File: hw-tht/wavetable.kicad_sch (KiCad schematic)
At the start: 33 parts, among them J8 SJ1-3535NG-GR, J9 Waveblaster, U10 74AHCT126, U11 NE5532, U7 74AHC00

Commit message: Mixer: +6 dB Waveblaster gain (R10/R11/R19/R20 20k, C30/C31 47p)
Waveblaster daughterboards put out about 1-1.2 Vrms full scale (DreamBlaster X2:
AK4388, 1.13 Vrms) against the PCM5100A's 2.1 Vrms, so with unity WT gain MIDI
was 5-6 dB quieter than PCM at RV1 max.

Raise the summer's feedback and PCM input resistors from 10k to 20k on both
boards: WT gain at RV1 max = 20k/10k = 2 (+6 dB), PCM 20k/20.47k (-0.2 dB, as
before). The daughterboard load (about 4.8k at RV1 max) and the pot taper stay
unchanged. C30/C31 100p -> 47p keeps the feedback pole at ~170 kHz.

BOM-only change (no copper change): schematic values/fields, PCB values,
BOM-THT/BOM-SMD lines with the previous values in the notes, DigiKey upload
files (1x/10x), schematic PDFs. SMD C30/C31 get an LCSC field (C14857,
CL21C470JBANNNC) because DigiKey only stocks the 100 V CL21C470JC61PNC.
README mixer text updated; the THT diagram now shows R14 on the J9 side of C22
and R12 joined to the summing node. ERC 0, DRC 0 with schematic parity.

Co-Authored-By: Claude Opus 5.5 <noreply@anthropic.com>
Claude-Session: https://claude.ai/code/session_011utN3x8yYUNDvkpGCEq5yD
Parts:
- C30, C31: value 100pF C0G -> 47pF C0G; Alternatives TDK FG28C0G1H101JNT06 (DK 445-173472-1-ND). -> TDK FG28C0G1H470JNT06 (DK 445-173499-1-ND); LCSC C123159 (T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; DigiKey BC1042CT-ND -> BC1038CT-ND; LCSC C400081 (TORCH CC4-0805-CG-100V-100PF-J (5.08 mm pitch)) -> C3690607; MPN K101J15C0GF5TH5 -> K470J15C0GF5TH5
- R10, R11, R19, R20: value 10K -> 20K; DigiKey 10.0KXBK-ND -> 20.0KXBK-ND; LCSC C1519255 -> C1364283; MPN MFR-25FBF52-10K -> MFR-25FBF52-20K
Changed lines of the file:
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@@
 			)
 		)
-		(property "Value" "10K"
+		(property "Value" "20K"
 			(at 167.64 93.98 90)
 			(show_name no)
@@
 			)
 		)
-		(property "Description" "10k 1/4W 1% metal film"
+		(property "Description" "20k 1/4W 1% metal film"
 			(at 167.64 91.44 0)
 			(hide yes)
@@
 			)
 		)
-		(property "MPN" "MFR-25FBF52-10K"
+		(property "MPN" "MFR-25FBF52-20K"
 			(at 167.64 91.44 0)
 			(hide yes)
@@
 			)
 		)
-		(property "DigiKey" "10.0KXBK-ND"
+		(property "DigiKey" "20.0KXBK-ND"
 			(at 167.64 91.44 0)
 			(hide yes)
@@
 			)
 		)
-		(property "LCSC" "C1519255"
+		(property "LCSC" "C1364283"
 			(at 167.64 91.44 0)
 			(hide yes)
@@
 			)
 		)
-		(property "Value" "10K"
+		(property "Value" "20K"
 			(at 193.04 88.04 90)
 			(show_name no)
@@
 			)
 		)
-		(property "Description" "10k 1/4W 1% metal film"
+		(property "Description" "20k 1/4W 1% metal film"
 			(at 187.96 86.36 0)
 			(hide yes)
@@
 			)
 		)
-		(property "MPN" "MFR-25FBF52-10K"
+		(property "MPN" "MFR-25FBF52-20K"
 			(at 187.96 86.36 0)
 			(hide yes)
@@
 			)
 		)
-		(property "DigiKey" "10.0KXBK-ND"
+		(property "DigiKey" "20.0KXBK-ND"
 			(at 187.96 86.36 0)
 			(hide yes)
@@
 			)
 		)
-		(property "LCSC" "C1519255"
+		(property "LCSC" "C1364283"
 			(at 187.96 86.36 0)
 			(hide yes)
@@
 			)
 		)
-		(property "Value" "100pF C0G"
+		(property "Value" "47pF C0G"
 			(at 186.69 77.47 90)
 			(show_name no)
@@
 			)
 		)
-		(property "Description" "100pF 50V C0G radial MLCC"
+		(property "Description" "47pF 50V C0G radial MLCC"
 			(at 187.96 81.28 0)
 			(hide yes)
@@
 			)
 		)
-		(property "MPN" "K101J15C0GF5TH5"
+		(property "MPN" "K470J15C0GF5TH5"
 			(at 187.96 81.28 0)
 			(hide yes)
@@
 			)
 		)
-		(property "DigiKey" "BC1042CT-ND"
+		(property "DigiKey" "BC1038CT-ND"
 			(at 187.96 81.28 0)
 			(hide yes)
@@
 			)
 		)
-		(property "LCSC" "C400081 (TORCH CC4-0805-CG-100V-100PF-J (5.08 mm pitch))"
+		(property "LCSC" "C3690607"
 			(at 187.96 81.28 0)
 			(hide yes)
@@
 			)
 		)
-		(property "Alternatives" "TDK FG28C0G1H101JNT06 (DK 445-173472-1-ND)."
+		(property "Alternatives" "TDK FG28C0G1H470JNT06 (DK 445-173499-1-ND); LCSC C123159 (TORCH CC4-0805-CG-50V-47pF-J, 5.08 mm pitch)."
 			(at 187.96 81.28 0)
 			(hide yes)
@@
 			)
 		)
-		(property "Value" "10K"
+		(property "Value" "20K"
 			(at 167.64 129.54 90)
 			(show_name no)
@@
 			)
 		)
-		(property "Description" "10k 1/4W 1% metal film"
+		(property "Description" "20k 1/4W 1% metal film"
 			(at 167.64 127 0)
 			(hide yes)
@@
 			)
 		)
-		(property "MPN" "MFR-25FBF52-10K"
+		(property "MPN" "MFR-25FBF52-20K"
 			(at 167.64 127 0)
 			(hide yes)
@@
 			)
 		)
-		(property "DigiKey" "10.0KXBK-ND"
+		(property "DigiKey" "20.0KXBK-ND"
 			(at 167.64 127 0)
 			(hide yes)
@@
 			)
 		)
-		(property "LCSC" "C1519255"
+		(property "LCSC" "C1364283"
 			(at 167.64 127 0)
 			(hide yes)
@@
 			)
 		)
-		(property "Value" "10K"
+		(property "Value" "20K"
 			(at 193.04 123.6 90)
 			(show_name no)
@@
 			)
 		)
-		(property "Description" "10k 1/4W 1% metal film"
+		(property "Description" "20k 1/4W 1% metal film"
 			(at 187.96 121.92 0)
 			(hide yes)
@@
 			)
 		)
-		(property "MPN" "MFR-25FBF52-10K"
+		(property "MPN" "MFR-25FBF52-20K"
 			(at 187.96 121.92 0)
 			(hide yes)
@@
 			)
 		)
-		(property "DigiKey" "10.0KXBK-ND"
+		(property "DigiKey" "20.0KXBK-ND"
 			(at 187.96 121.92 0)
 			(hide yes)
@@
 			)
 		)
-		(property "LCSC" "C1519255"
+		(property "LCSC" "C1364283"
 			(at 187.96 121.92 0)
 			(hide yes)
@@
 			)
 		)
-		(property "Value" "100pF C0G"
+		(property "Value" "47pF C0G"
 			(at 186.69 113.03 90)
 			(show_name no)
@@
 			)
 		)
-		(property "Description" "100pF 50V C0G radial MLCC"
+		(property "Description" "47pF 50V C0G radial MLCC"
 			(at 187.96 116.84 0)
 			(hide yes)
@@
 			)
 		)
-		(property "MPN" "K101J15C0GF5TH5"
+		(property "MPN" "K470J15C0GF5TH5"
 			(at 187.96 116.84 0)
 			(hide yes)
@@
 			)
 		)
-		(property "DigiKey" "BC1042CT-ND"
+		(property "DigiKey" "BC1038CT-ND"
 			(at 187.96 116.84 0)
 			(hide yes)
@@
 			)
 		)
-		(property "LCSC" "C400081 (TORCH CC4-0805-CG-100V-100PF-J (5.08 mm pitch))"
+		(property "LCSC" "C3690607"
 			(at 187.96 116.84 0)
 			(hide yes)
@@
 			)
 		)
-		(property "Alternatives" "TDK FG28C0G1H101JNT06 (DK 445-173472-1-ND)."
+		(property "Alternatives" "TDK FG28C0G1H470JNT06 (DK 445-173499-1-ND); LCSC C123159 (TORCH CC4-0805-CG-50V-47pF-J, 5.08 mm pitch)."
 			(at 187.96 116.84 0)
 			(hide yes)

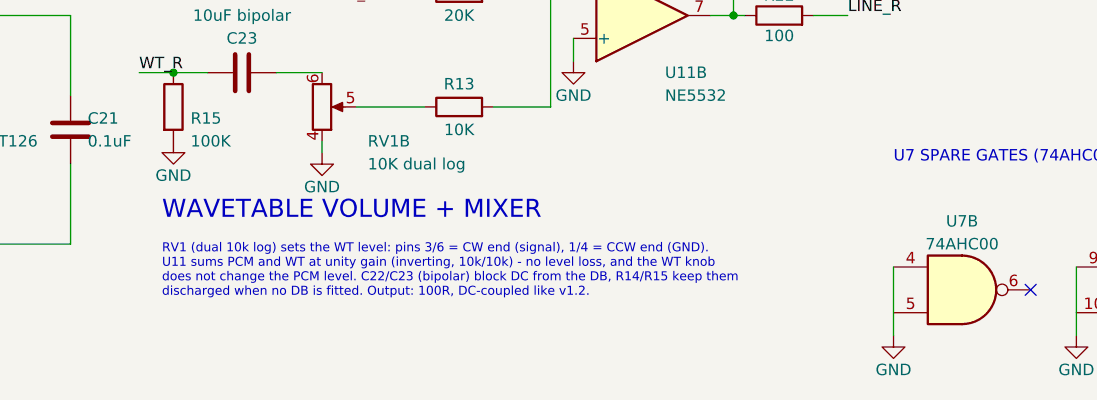
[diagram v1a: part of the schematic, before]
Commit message: Mixer docs: schematic note, DAC load and wording for the +6 dB WT gain
Review fixes for e33fce5:
- The wavetable-sheet note (both boards, and the schematic PDFs) still said
  "unity gain (inverting, 10k/10k)". It now gives PCM 20k/20k (~unity) and
  WT x2 (+6 dB), wrapped so it stays clear of the THT spare U7 gates.
- THT README: the PCM510x now sees ~20.5k (R7 + R10), not ~10.5k.
- Wording: the 47p corner is ~170 kHz (was ~160 kHz with 10k/100p), PCM gain
  moves -0.4 -> -0.2 dB ("essentially unchanged"), and keeping 100p costs
  ~0.2 dB more at 20 kHz. Same wording in the BOM notes.

Co-Authored-By: Claude Opus 5.5 <noreply@anthropic.com>
Claude-Session: https://claude.ai/code/session_011utN3x8yYUNDvkpGCEq5yD
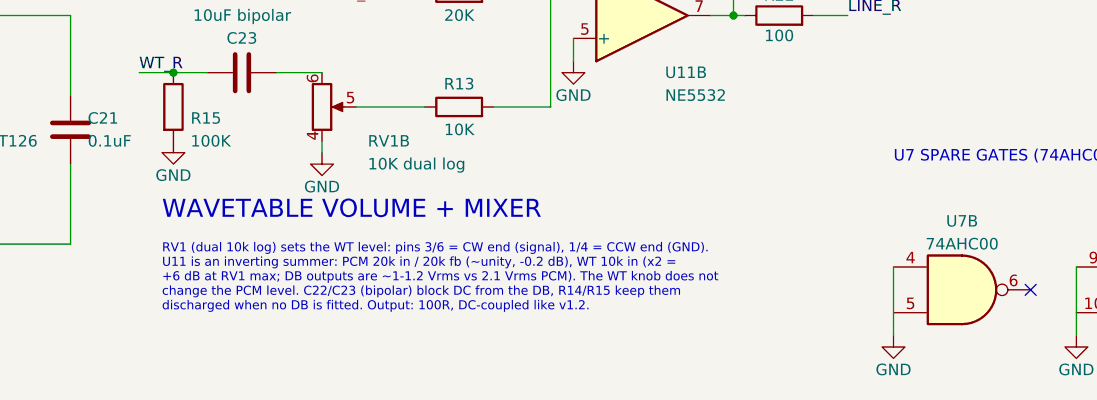
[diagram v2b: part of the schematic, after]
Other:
- note added: "RV1 (dual 10k log) sets the WT level: pins 3/6 = CW end (signal), 1/4 = CCW end (GND). U11 is an inverting summer: PCM 20k in / 20k fb (~unity, -0.2 dB), WT 10k in (x2 = +6 dB at RV1 max; DB outputs are ~1-1.2 Vrms vs 2.1 Vrms PCM). The WT knob does not change the PCM level. C22/C23 (bipolar) block DC from the DB, R14/R15 keep them discharged when no DB is fitted. Output: 100R, DC-coupled like v1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"
- note removed: "RV1 (dual 10k log) sets the WT level: pins 3/6 = CW end (signal), 1/4 = CCW end (GND). U11 sums PCM and WT at unity gain (inverting, 10k/10k) - no level loss, and the WT knob does not change the PCM level. C22/C23 (bipolar) block DC from the DB, R14/R15 keep them discharged when no DB is fitted. Output: 100R, DC-coupled like v1.2."
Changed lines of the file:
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@@
 		)
 	)
-	(text "RV1 (dual 10k log) sets the WT level: pins 3/6 = CW end (signal), 1/4 = CCW end (GND).\nU11 sums PCM and WT at unity gain (inverting, 10k/10k) - no level loss, and the WT knob\ndoes not change the PCM level. C22/C23 (bipolar) block DC from the DB, R14/R15 keep them\ndischarged when no DB is fitted. Output: 100R, DC-coupled like v1.2."
+	(text "RV1 (dual 10k log) sets the WT level: pins 3/6 = CW end (signal), 1/4 = CCW end (GND).\nU11 is an inverting summer: PCM 20k in / 20k fb (~unity, -0.2 dB), WT 10k in (x2 =\n+6 dB at RV1 max; DB outputs are ~1-1.2 Vrms vs 2.1 Vrms PCM). The WT knob does not\nchange the PCM level. C22/C23 (bipolar) block DC from the DB, R14/R15 keep them\ndischarged when no DB is fitted. Output: 100R, DC-coupled like v1.2."
 		(exclude_from_sim no)
 		(at 134.62 154.94 0)
